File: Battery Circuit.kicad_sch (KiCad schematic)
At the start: 43 parts, among them J1 1827685-4, J2 Programming Header (SWD), Q1 Si2309DS, Q2 BC847, SW1 SW_Push, U1 TPS54202DDC, U2 STM32G071KBUxN

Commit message: Fixed voltage divider: Updated R12 to 32.4k to ensure safe 3.3V output
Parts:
- R12: value 22.1kΩ -> 32.4kΩ
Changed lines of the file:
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@@
 			)
 		)
-		(property "Value" "22.1kΩ"
+		(property "Value" "32.4kΩ"
 			(at 249.174 149.86 0)
 			(show_name no)

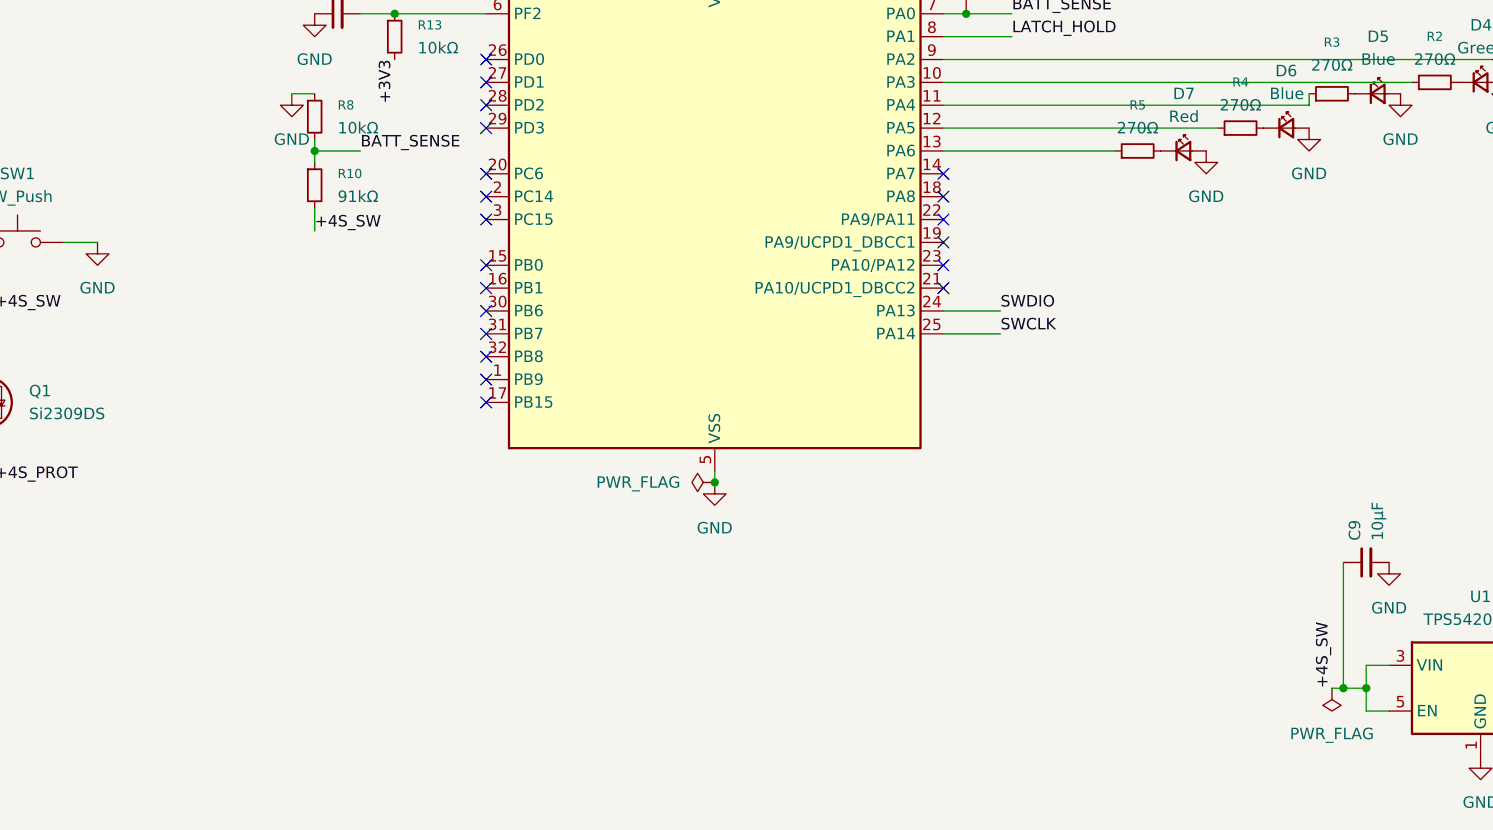
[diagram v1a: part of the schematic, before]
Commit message: Finalize 4-layer PCB layout: implement 20A top/bottom copper pours, add via stitching, addition of thermistor and clear all DRC violations.
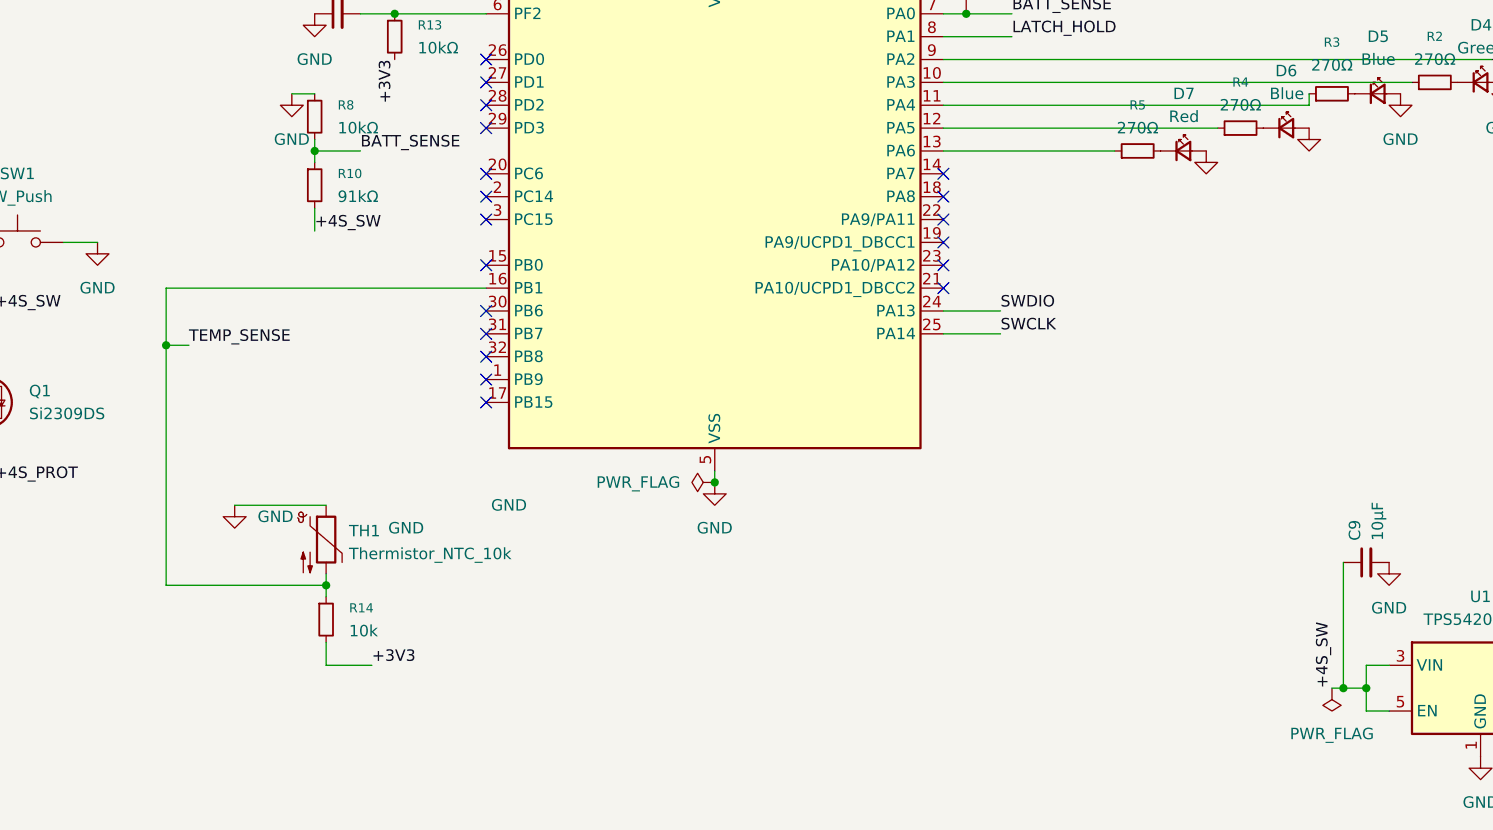
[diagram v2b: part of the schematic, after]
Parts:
- added R14: 10k, Resistor_SMD:R_01005_0402Metric, symbol Device:R_Small
- added TH1: Thermistor_NTC_10k, Resistor_SMD:R_01005_0402Metric, symbol Device:Thermistor_NTC
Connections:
- net +3V3: now also R14.2
- net GND: now also TH1.1
- net TEMP_SENSE: now reaches U2.16 (PB1)
- net TEMP_SENSE: now also R14.1, TH1.2
- no-connect marks 20 -> 19

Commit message: feat(system): implement BMS firmware
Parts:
- D5, D6: value Blue -> Green
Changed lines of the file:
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@@
 			)
 		)
-		(property "Value" "Blue"
+		(property "Value" "Green"
 			(at 215.9635 69.85 0)
 			(show_name no)
@@
 			)
 		)
-		(property "Value" "Blue"
+		(property "Value" "Green"
 			(at 226.1235 66.04 0)
 			(show_name no)

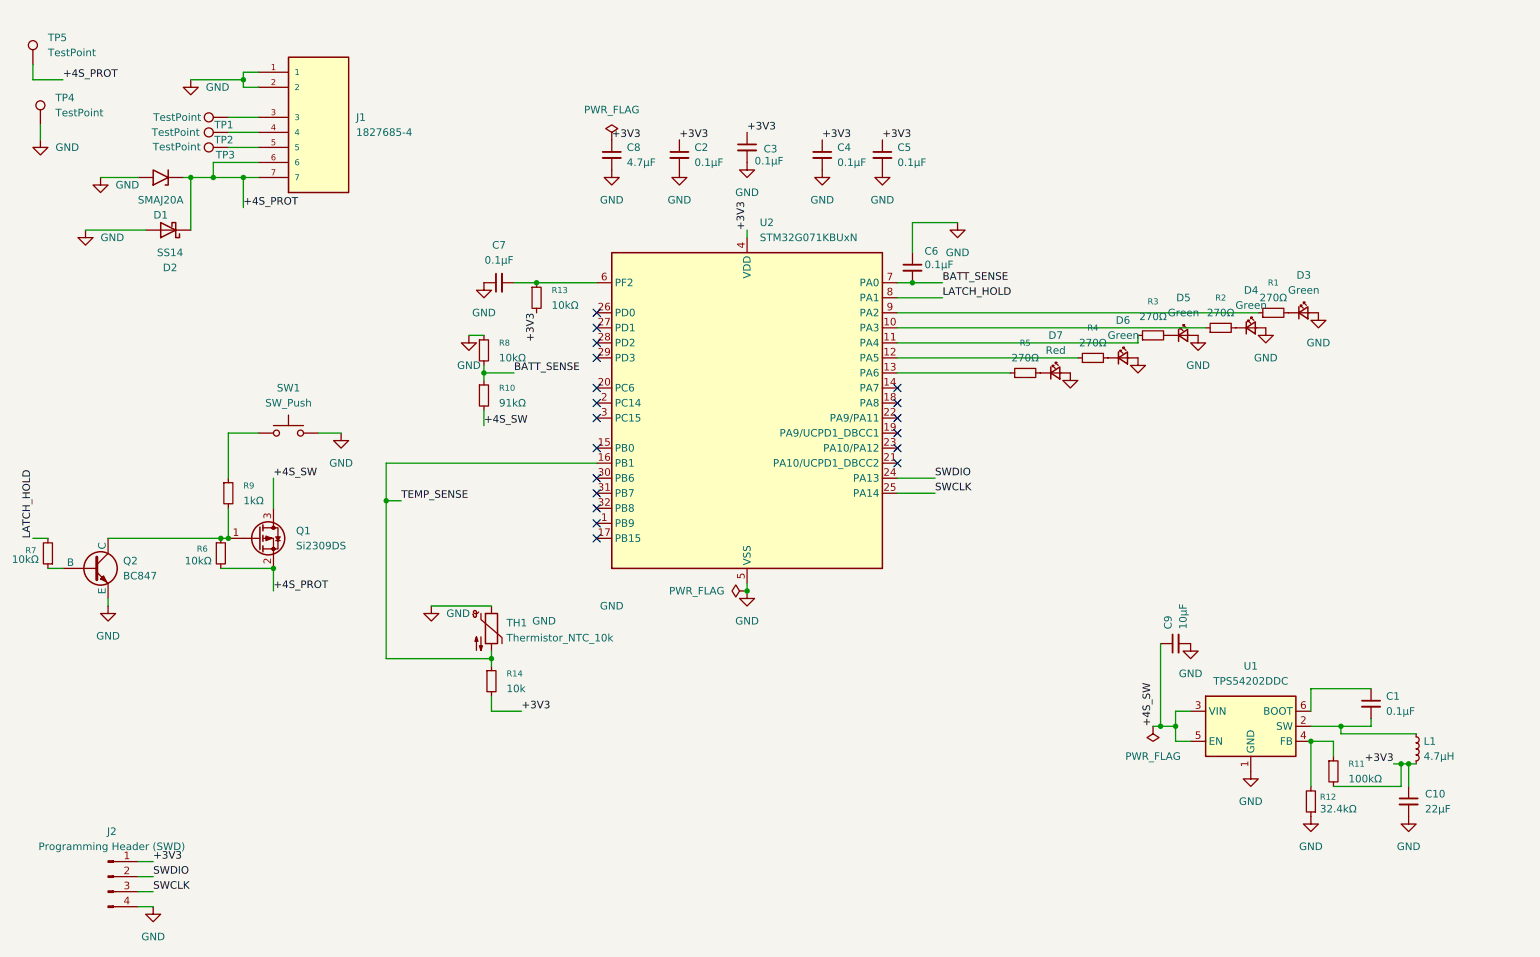
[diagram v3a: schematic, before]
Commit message: feat(system): GERBER File & BOM with STM32G071GBU6N MCU
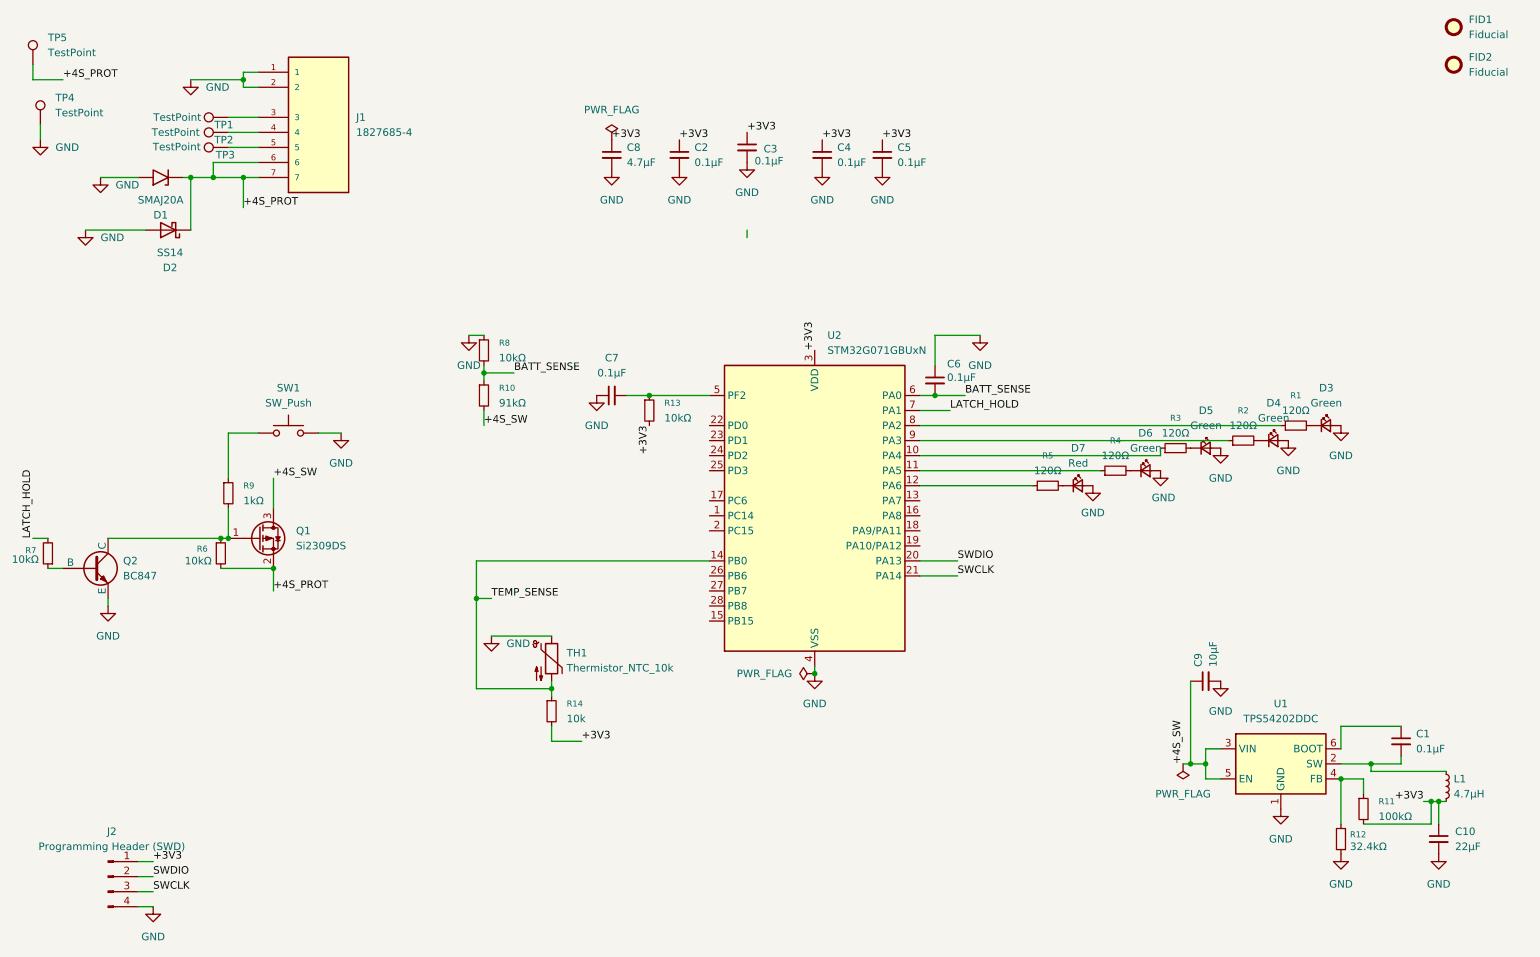
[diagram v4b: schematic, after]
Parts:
- removed U2: STM32G071KBUxN, Package_DFN_QFN:QFN-32-1EP_5x5mm_P0.5mm_EP3.45x3.45mm, symbol MCU_ST_STM32G0:STM32G071KBUxN
- added FID1, FID2: Fiducial, Fiducial:Fiducial_1mm_Mask2mm, symbol Mechanical:Fiducial
- added U2: STM32G071GBUxN, Package_DFN_QFN:QFN-28_4x4mm_P0.5mm, symbol MCU_ST_STM32G0:STM32G071GBUxN
- R1, R2, R3, R4, R5: value 270Ω -> 120Ω
- R14, TH1: footprint Resistor_SMD:R_01005_0402Metric -> Resistor_SMD:R_0402_1005Metric
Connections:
- net +3V3: now also U2.3 (VDD)
- net BATT_SENSE: now also U2.6 (PA0)
- net GND: now also U2.4 (VSS)
- net LATCH_HOLD: now also U2.7 (PA1)
- net SWCLK: now also U2.21 (PA14)
- net SWDIO: now also U2.20 (PA13)
- net TEMP_SENSE: now also U2.14 (PB0)
- net at R4.1: now also U2.11 (PA5)
- net at R3.1: now also U2.10 (PA4)
- net at R5.1: now also U2.12 (PA6)
- net at C7.2, R13.1: now also U2.5 (PF2)
- net at R2.1: now also U2.9 (PA3)
- net at R1.1: now also U2.8 (PA2)
- no-connect marks 19 -> 0
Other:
- moved on the sheet: C1, C10, C6, C7, C9, D3, D4, D5, D6, D7, L1, R1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

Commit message: Update hardware schematic to Rev 1.1 (fixed MOSFET/drain)
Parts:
- added R15: 10k, Resistor_SMD:R_0402_1005Metric, symbol Device:R_Small
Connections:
- net +4S_PROT: now also Q1.3 (D); no longer Q1.2 (S)
- net +4S_SW: now also Q1.2 (S); no longer Q1.3 (D)
- net GND: now also R15.1
- net at Q2.2 (B), R7.1: now also R15.2
